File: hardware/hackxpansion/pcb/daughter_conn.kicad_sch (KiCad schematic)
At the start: 1 part, among them CN1 533981471

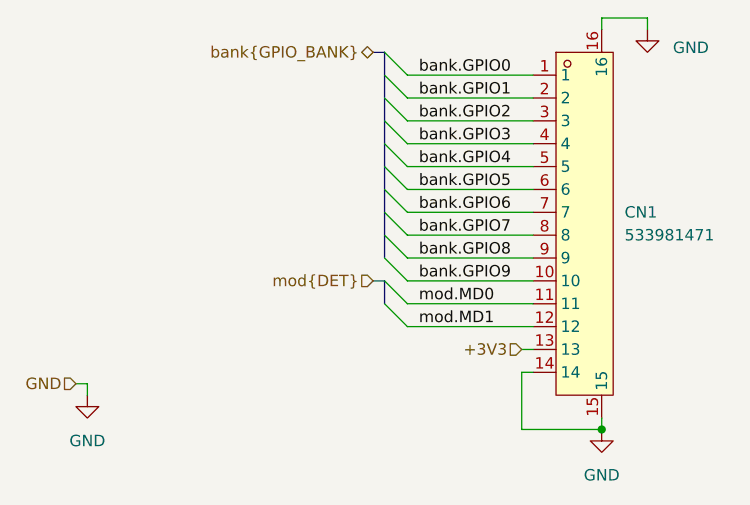
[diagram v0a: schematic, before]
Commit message: reordered shematic
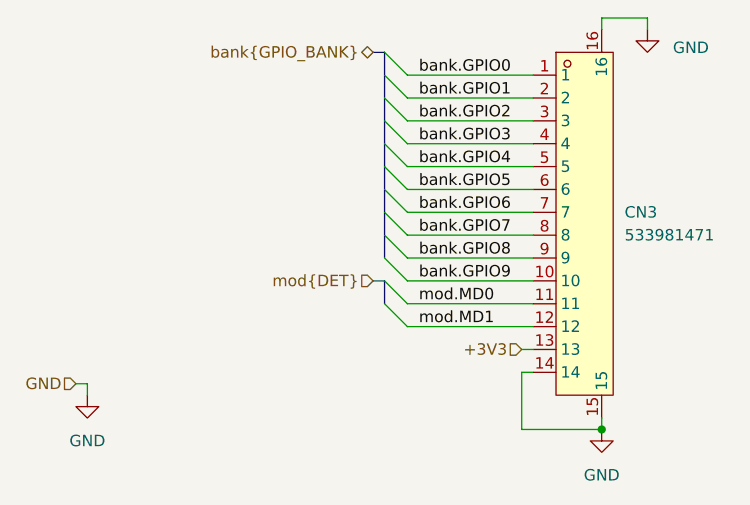
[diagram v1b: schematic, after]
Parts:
- renumbered CN1 to CN3
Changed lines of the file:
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@@
 		(dnp no)
 		(fields_autoplaced yes)
-		(property "Reference" "CN1"
+		(property "Reference" "CN3"
 			(at 163.83 67.3099 0)
 			(show_name no)
@@
 		(dnp no)
 		(fields_autoplaced yes)
-		(property "Reference" "#PWR032"
+		(property "Reference" "#PWR035"
 			(at 104.14 93.98 0)
 			(hide yes)
@@
 		(in_pos_files yes)
 		(dnp no)
-		(property "Reference" "#PWR0104"
+		(property "Reference" "#PWR0106"
 			(at 166.37 53.34 0)
 			(hide yes)
@@
 		(dnp no)
 		(fields_autoplaced yes)
-		(property "Reference" "#PWR044"
+		(property "Reference" "#PWR097"
 			(at 161.29 97.79 0)
 			(hide yes)
